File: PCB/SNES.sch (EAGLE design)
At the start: 22 parts, among them U1A SN74AHCT125N, U2A SN74AHCT125N, U3A SN74AHCT125N

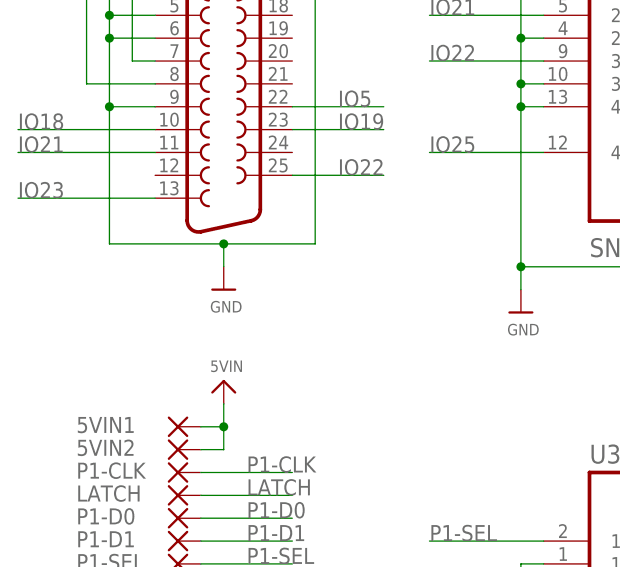
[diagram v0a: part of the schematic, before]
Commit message: Added exposed GND plane at DB25 anchors
All PCBs have been update to have exposed GND plane pads for the DB25 anchor points.

This resolves Issue 54
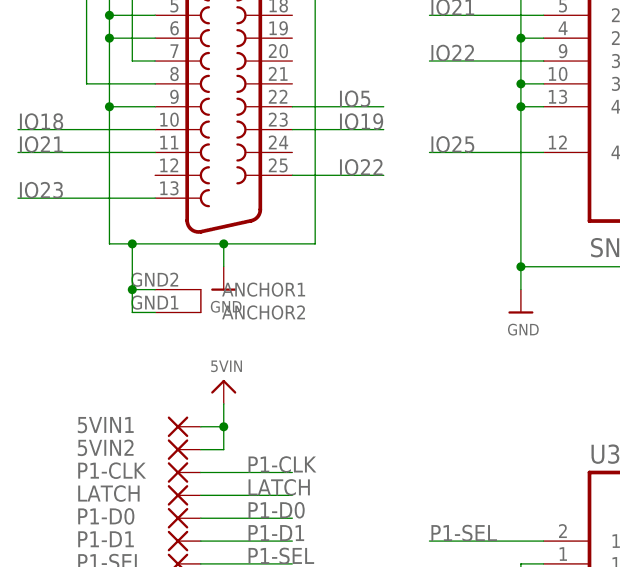
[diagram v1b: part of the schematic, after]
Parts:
- X1: device SparkFun-Retired:DB25_FEMALEH -> SparkFun-Retired:DB25_FEMALEHP
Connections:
- net GND: now also X1.ANCHOR1, X1.ANCHOR2
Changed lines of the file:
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@@
 </classes>
 <parts>
-<part name="X1" library="SparkFun-Retired" deviceset="DB25_FEMALE" device="H"/>
+<part name="X1" library="SparkFun-Retired" deviceset="DB25_FEMALE" device="HP"/>
 <part name="U$43" library="microbuilder" deviceset="VIN" device="" value="3V3IN"/>
 <part name="U$44" library="microbuilder" deviceset="VIN" device="" value="5VIN"/>
@@
 <wire x1="238.76" y1="-109.22" x2="238.76" y2="-111.76" width="0.1524" layer="91"/>
 <junction x="238.76" y="-109.22"/>
-<wire x1="238.76" y1="-109.22" x2="226.06" y2="-109.22" width="0.1524" layer="91"/>
+<wire x1="238.76" y1="-109.22" x2="228.6" y2="-109.22" width="0.1524" layer="91"/>
 <pinref part="X1" gate="-1" pin="9"/>
+<wire x1="228.6" y1="-109.22" x2="226.06" y2="-109.22" width="0.1524" layer="91"/>
 <wire x1="231.14" y1="-93.98" x2="226.06" y2="-93.98" width="0.1524" layer="91"/>
 <wire x1="226.06" y1="-93.98" x2="226.06" y2="-109.22" width="0.1524" layer="91"/>
@@
 <wire x1="246.38" y1="-81.28" x2="248.92" y2="-81.28" width="0.1524" layer="91"/>
 <junction x="248.92" y="-81.28"/>
+<pinref part="X1" gate="-1" pin="ANCHOR2"/>
+<wire x1="231.14" y1="-116.84" x2="228.6" y2="-116.84" width="0.1524" layer="91"/>
+<wire x1="228.6" y1="-116.84" x2="228.6" y2="-114.3" width="0.1524" layer="91"/>
+<junction x="228.6" y="-109.22"/>
+<pinref part="X1" gate="-1" pin="ANCHOR1"/>
+<wire x1="228.6" y1="-114.3" x2="228.6" y2="-109.22" width="0.1524" layer="91"/>
+<wire x1="231.14" y1="-114.3" x2="228.6" y2="-114.3" width="0.1524" layer="91"/>
+<junction x="228.6" y="-114.3"/>
 </segment>
 <segment>
